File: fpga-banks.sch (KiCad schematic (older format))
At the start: 52 parts, among them J13 62000311121, Q12 2N7002, Q13 2N7002, Q14 2N7002, Q15 2N7002, Q16 2N7002, U14 XC7A100T-FGG484

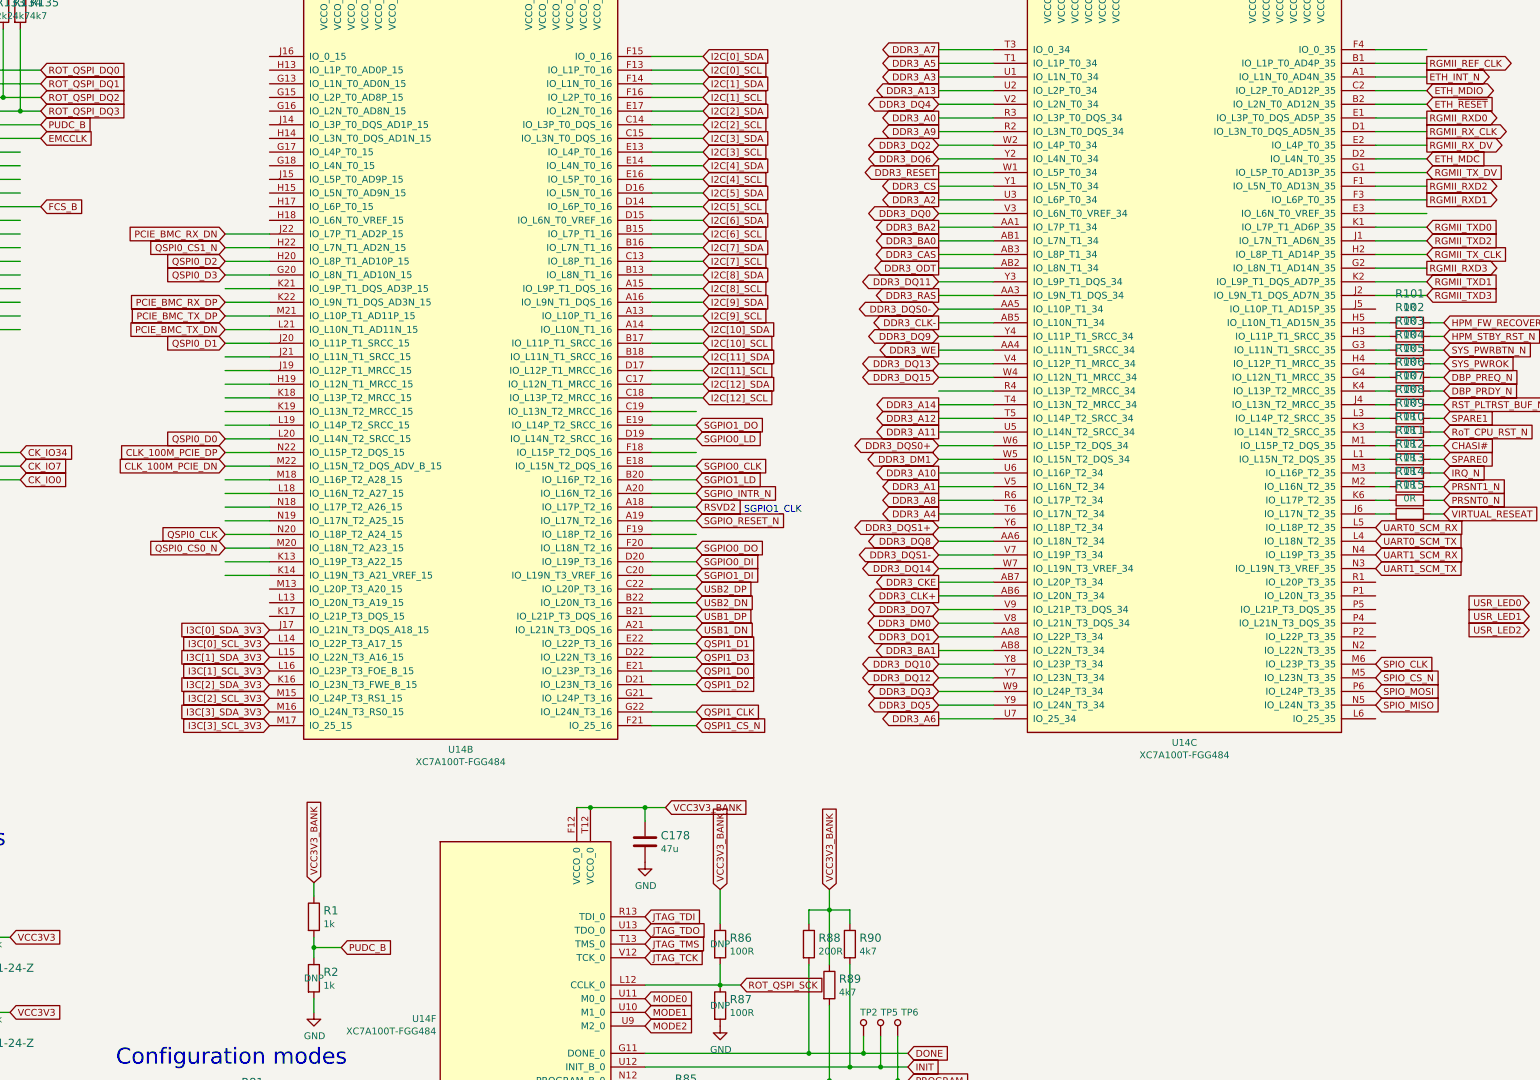
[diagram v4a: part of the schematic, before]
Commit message: Reconnected DDR3
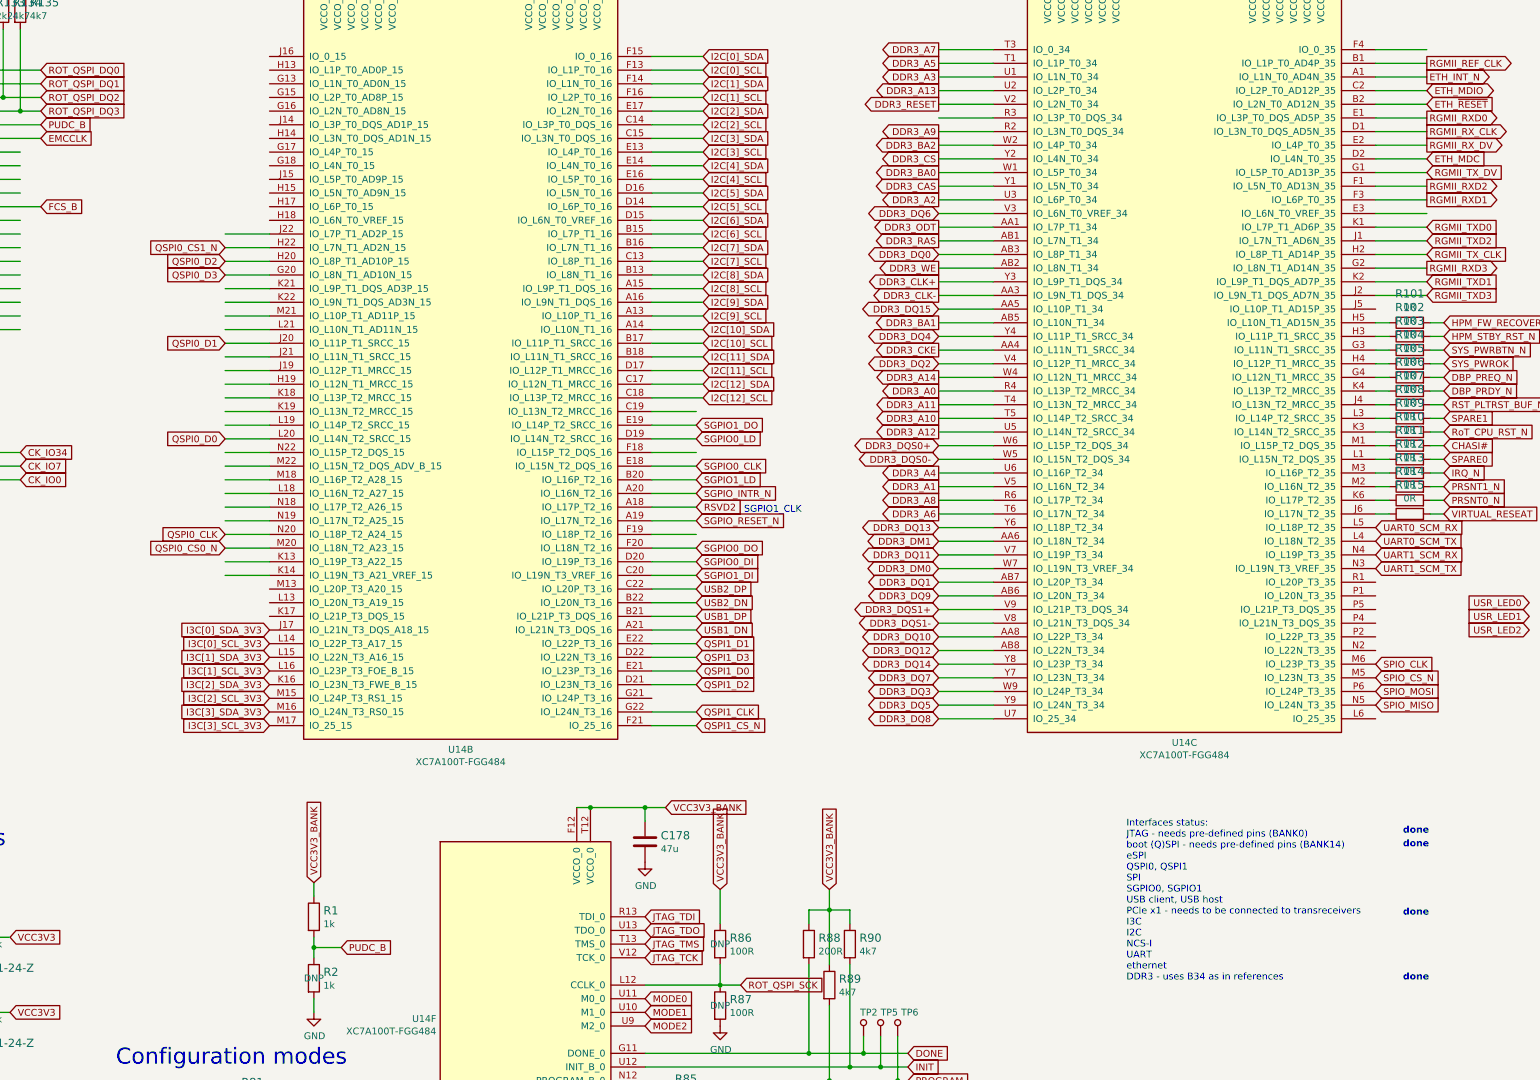
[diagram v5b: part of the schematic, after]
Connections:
- net labels removed: CLK_100M_PCIE_DN, CLK_100M_PCIE_DP, PCIE_BMC_RX_DN, PCIE_BMC_RX_DP, PCIE_BMC_TX_DN, PCIE_BMC_TX_DP
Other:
- note added: "Interfaces status:\nJTAG - needs pre-defined pins (BANK0)\nboot (Q)SPI - needs pre-defined pins (BANK14)\neSPI\nQSPI0, QSPI1\nSPI\nSGPIO0, SGPIO1\nUSB client, USB host\nPCIe x1 - needs to be connected to transreceivers\nI3C\nI2C\nNCS-I\nUART\nethernet\nDDR3 - uses B34 as in references"
- note added: "done"
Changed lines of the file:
@@
 Text GLabel 4850 975  2    50   Input ~ 0
 VCC1V8_BANK
-Text GLabel 6375 4950 0    50   Input ~ 0
-CLK_100M_PCIE_DP
-Text GLabel 6375 5050 0    50   Input ~ 0
-CLK_100M_PCIE_DN
-Text GLabel 6375 3950 0    50   Input ~ 0
-PCIE_BMC_TX_DP
-Text GLabel 6375 4050 0    50   Input ~ 0
-PCIE_BMC_TX_DN
-Text GLabel 6375 3350 0    50   Input ~ 0
-PCIE_BMC_RX_DN
-Text GLabel 6375 3850 0    50   Input ~ 0
-PCIE_BMC_RX_DP
 Text GLabel 6700 6250 0    50   Input ~ 0
 I3C[0]_SDA_3V3
@@
 Wire Wire Line
 	6375 3650 6700 3650
-Text GLabel 6375 3450 0    50   Input ~ 0
-QSPI0_CS1_N
 Text GLabel 9825 6350 2    50   Input ~ 0
 QSPI1_D1
@@
 Text GLabel 11600 2300 0    50   Output ~ 0
 DDR3_A13
+Text GLabel 11600 4800 0    50   Output ~ 0
+DDR3_A12
+Text GLabel 11600 4600 0    50   Output ~ 0
+DDR3_A11
 Text GLabel 11600 4700 0    50   Output ~ 0
-DDR3_A12
-Text GLabel 11600 4800 0    50   Output ~ 0
-DDR3_A11
-Text GLabel 11600 5100 0    50   Output ~ 0
 DDR3_A10
-Text GLabel 11600 2900 0    50   Output ~ 0
+Text GLabel 11600 2400 0    50   Output ~ 0
 DDR3_RESET
-Text GLabel 11600 5900 0    50   Output ~ 0
+Text GLabel 11600 4200 0    50   Output ~ 0
 DDR3_CKE
-Text GLabel 11600 4000 0    50   Output ~ 0
+Text GLabel 11600 3800 0    50   Output ~ 0
 DDR3_CLK-
-Text GLabel 11600 6000 0    50   Output ~ 0
+Text GLabel 11600 3700 0    50   Output ~ 0
 DDR3_CLK+
-Text GLabel 11600 2500 0    50   Output ~ 0
+Text GLabel 11600 4500 0    50   Output ~ 0
 DDR3_A0
 Text GLabel 11600 5200 0    50   Output ~ 0
@@
 Text GLabel 11600 2200 0    50   Output ~ 0
 DDR3_A3
-Text GLabel 11600 5400 0    50   Output ~ 0
+Text GLabel 11600 5100 0    50   Output ~ 0
 DDR3_A4
 Text GLabel 11600 2100 0    50   Output ~ 0
 DDR3_A5
-Text GLabel 11600 6900 0    50   Output ~ 0
+Text GLabel 11600 5400 0    50   Output ~ 0
 DDR3_A6
 Text GLabel 11600 2000 0    50   Output ~ 0
@@
 Text GLabel 11600 2600 0    50   Output ~ 0
 DDR3_A9
+Text GLabel 11600 2900 0    50   Output ~ 0
+DDR3_BA0
+Text GLabel 11600 2700 0    50   Output ~ 0
+DDR3_BA2
+Text GLabel 11600 2800 0    50   Output ~ 0
+DDR3_CS
+Text GLabel 11600 3000 0    50   Output ~ 0
+DDR3_CAS
 Text GLabel 11600 3400 0    50   Output ~ 0
-DDR3_BA0
-Text GLabel 11600 6400 0    50   Output ~ 0
-DDR3_BA1
+DDR3_RAS
+Text GLabel 11600 3600 0    50   Output ~ 0
+DDR3_WE
 Text GLabel 11600 3300 0    50   Output ~ 0
-DDR3_BA2
-Text GLabel 11600 3000 0    50   Output ~ 0
-DDR3_CS
-Text GLabel 11600 3500 0    50   Output ~ 0
-DDR3_CAS
-Text GLabel 11600 3800 0    50   Output ~ 0
-DDR3_RAS
-Text GLabel 11600 4200 0    50   Output ~ 0
-DDR3_WE
-Text GLabel 11600 3600 0    50   Output ~ 0
 DDR3_ODT
-Text GLabel 11600 3200 0    50   BiDi ~ 0
+Text GLabel 11600 3500 0    50   BiDi ~ 0
 DDR3_DQ0
-Text GLabel 11600 6300 0    50   BiDi ~ 0
+Text GLabel 11600 5900 0    50   BiDi ~ 0
 DDR3_DQ1
-Text GLabel 11600 2700 0    50   BiDi ~ 0
+Text GLabel 11600 4300 0    50   BiDi ~ 0
 DDR3_DQ2
 Text GLabel 11600 6700 0    50   BiDi ~ 0
 DDR3_DQ3
-Text GLabel 11600 2400 0    50   BiDi ~ 0
+Text GLabel 11600 4100 0    50   BiDi ~ 0
 DDR3_DQ4
 Text GLabel 11600 6800 0    50   BiDi ~ 0
 DDR3_DQ5
-Text GLabel 11600 2800 0    50   BiDi ~ 0
+Text GLabel 11600 3200 0    50   BiDi ~ 0
 DDR3_DQ6
-Text GLabel 11600 6100 0    50   BiDi ~ 0
+Text GLabel 11600 6600 0    50   BiDi ~ 0
 DDR3_DQ7
-Text GLabel 11600 5600 0    50   BiDi ~ 0
+Text GLabel 11600 6900 0    50   BiDi ~ 0
 DDR3_DQ8
-Text GLabel 11600 4100 0    50   BiDi ~ 0
+Text GLabel 11600 6000 0    50   BiDi ~ 0
 DDR3_DQ9
-Text GLabel 11600 6500 0    50   BiDi ~ 0
+Text GLabel 11600 6300 0    50   BiDi ~ 0
 DDR3_DQ10
-Text GLabel 11600 3700 0    50   BiDi ~ 0
+Text GLabel 11600 5700 0    50   BiDi ~ 0
 DDR3_DQ11
-Text GLabel 11600 6600 0    50   BiDi ~ 0
+Text GLabel 11600 6400 0    50   BiDi ~ 0
 DDR3_DQ12
-Text GLabel 11600 4400 0    50   BiDi ~ 0
+Text GLabel 11600 3900 0    50   BiDi ~ 0
 DDR3_DQ15
-Text GLabel 11600 6200 0    50   BiDi ~ 0
+Text GLabel 11600 5800 0    50   BiDi ~ 0
 DDR3_DM0
-Text GLabel 11600 5000 0    50   BiDi ~ 0
-DDR3_DM1
 Text GLabel 11600 4900 0    50   BiDi ~ 0
 DDR3_DQS0+
-Text GLabel 11600 3900 0    50   BiDi ~ 0
+Text GLabel 11600 5000 0    50   BiDi ~ 0
 DDR3_DQS0-
+Text GLabel 11600 6100 0    50   BiDi ~ 0
+DDR3_DQS1+
+Text GLabel 11600 6200 0    50   BiDi ~ 0
+DDR3_DQS1-
+Wire Wire Line
+	11600 3200 12000 3200
 Text GLabel 11600 5500 0    50   BiDi ~ 0
-DDR3_DQS1+
-Text GLabel 11600 5700 0    50   BiDi ~ 0
-DDR3_DQS1-
-Wire Wire Line
-	11600 3200 12000 3200
-Text GLabel 11600 4300 0    50   BiDi ~ 0
 DDR3_DQ13
-Text GLabel 11600 5800 0    50   BiDi ~ 0
+Text GLabel 11600 6500 0    50   BiDi ~ 0
 DDR3_DQ14
-Text GLabel 11600 4600 0    50   Output ~ 0
+Text GLabel 11600 4400 0    50   Output ~ 0
 DDR3_A14
 Text GLabel 1575 7600 2    50   Input ~ 0
@@
 Text GLabel 1225 9400 0    50   Input ~ 0
 GPX_USB2
+Text Notes 12975 8825 0    50   ~ 0
+Interfaces status:\nJTAG - needs pre-defined pins (BANK0)\nboot (Q)SPI - needs pre-defined pins (BANK14)\neSPI\nQSPI0, QSPI1\nSPI\nSGPIO0, SGPIO1\nUSB client, USB host\nPCIe x1 - needs to be connected to transreceivers\nI3C\nI2C\nNCS-I\nUART\nethernet\nDDR3 - uses B34 as in references
+Text Notes 15000 7750 0    50   ~ 10
+done
+Text Notes 15000 7850 0    50   ~ 10
+done
+Text GLabel 6375 3450 0    50   Input ~ 0
+QSPI0_CS1_N
+Text Notes 15000 8350 0    50   ~ 10
+done
+Text GLabel 11600 5600 0    50   BiDi ~ 0
+DDR3_DM1
+Text GLabel 11600 4000 0    50   Output ~ 0
+DDR3_BA1
+Text Notes 15000 8825 0    50   ~ 10
+done
 $EndSCHEMATC
